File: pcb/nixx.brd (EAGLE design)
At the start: 20 x 40 mm, 43 parts, among them IC1 24C64ST

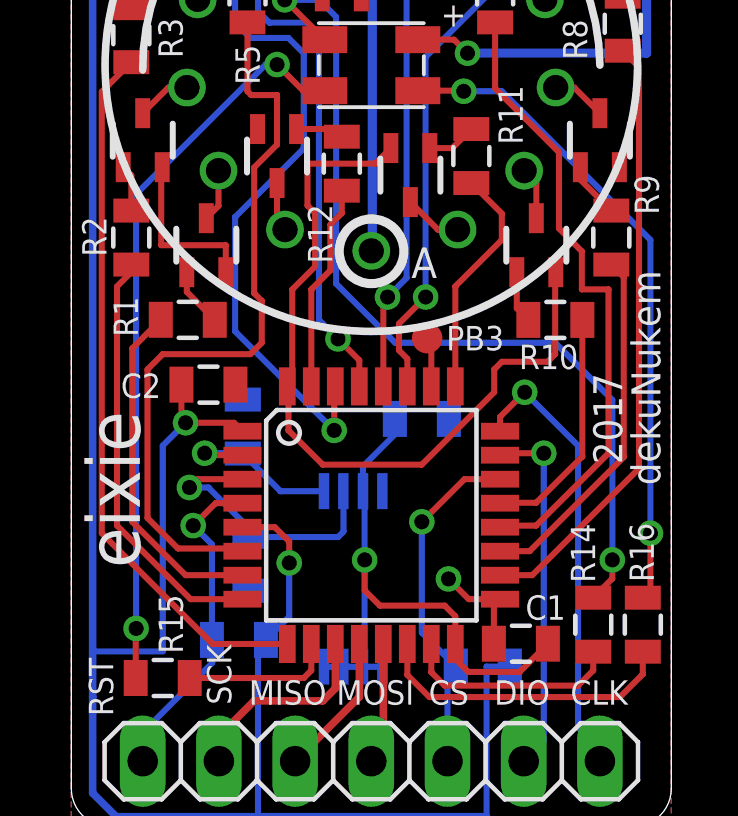
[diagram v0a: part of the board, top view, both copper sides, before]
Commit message: using NSS, SPI test
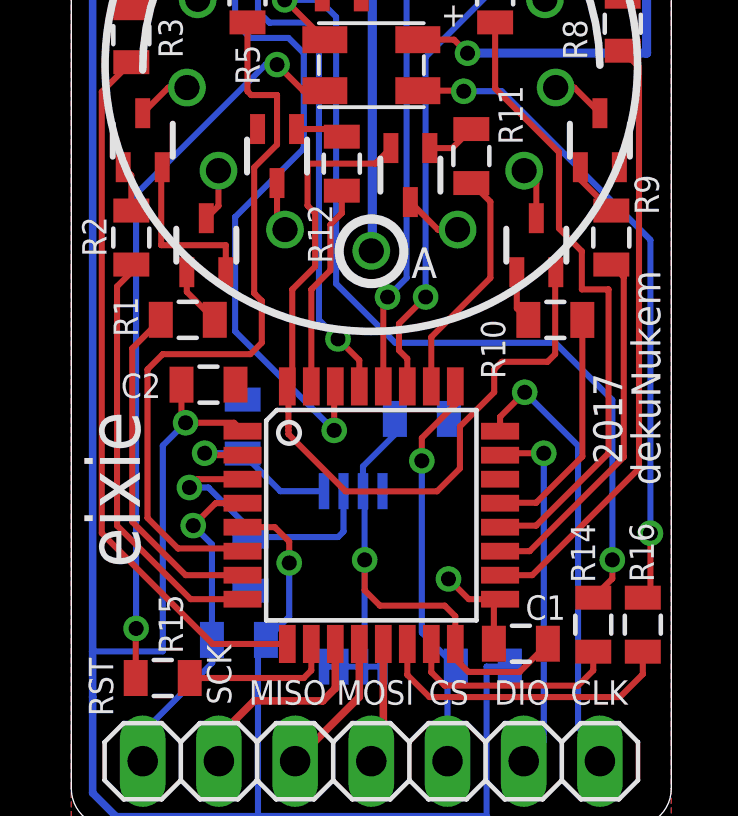
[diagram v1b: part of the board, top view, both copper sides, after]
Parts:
- removed TP3: TEST-POINT3X4, joyAnalog:PAD.03X.04
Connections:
- removed net N$17: TP3.P$1, U$2.26
- net SPI_CS: now also U$2.25; no longer U$2.22
- net STM_DOT_LEFT: now also U$2.26; no longer U$2.25
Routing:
- net SPI_CS: track 11.8 -> 13.6 mm
- net N$17: track 1.67 -> 0.00 mm
- net GND: track 57.0 -> 58.6 mm
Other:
- board text removed: "PB3"
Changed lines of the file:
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@@
 <circle x="10.0076" y="19.177" radius="1.077628125" width="0.3048" layer="21"/>
 <text x="12.192" y="19.304" size="1.016" layer="25" rot="R180">A</text>
-<text x="12.4968" y="15.875" size="0.8128" layer="25">PB3</text>
 <text x="17.018" y="34.671" size="1.143" layer="25">G</text>
 <text x="18.669" y="18.542" size="0.9652" layer="25" rot="R270">dekuNukem</text>
@@
 </element>
 <element name="R10" library="joyAnalog" package="0805" value="" x="16.135" y="16.889" smashed="yes" rot="R180">
-<attribute name="NAME" x="16.897" y="16.0635" size="0.8128" layer="25" rot="R180"/>
+<attribute name="NAME" x="13.6545" y="16.897" size="0.8128" layer="25" rot="R270"/>
 <attribute name="VALUE" x="17.151" y="18.286" size="0.4064" layer="27" rot="R180"/>
 <attribute name="VALUE" x="17.151" y="18.286" size="0.4064" layer="27" rot="R180"/>
@@
 <attribute name="VALUE" x="17.653" y="7.747" size="0.4064" layer="27" rot="R270"/>
 </element>
-<element name="TP3" library="joyAnalog" package="PAD.03X.04" value="TEST-POINT3X4" x="11.8618" y="16.2814" smashed="yes"/>
 <element name="R17" library="joyAnalog" package="0805" value="" x="5.588" y="6.223" smashed="yes" rot="MR180">
 <attribute name="NAME" x="4.7244" y="5.2197" size="0.8128" layer="26" rot="MR180"/>
@@
 <wire x1="13.2334" y1="5.1562" x2="12.8" y2="5.5896" width="0.2032" layer="1"/>
 <wire x1="12.8" y1="5.5896" x2="12.8" y2="6.0884" width="0.2032" layer="1"/>
-<wire x1="14.097" y1="14.478" x2="11.684" y2="12.065" width="0.2032" layer="1"/>
-<wire x1="11.684" y1="12.065" x2="8.382" y2="12.065" width="0.2032" layer="1"/>
-<wire x1="8.382" y1="12.065" x2="7.239" y2="13.208" width="0.2032" layer="1"/>
-<wire x1="7.239" y1="13.208" x2="7.239" y2="14.605" width="0.2032" layer="1"/>
+<wire x1="7.239" y1="13.208" x2="7.239" y2="13.335" width="0.2032" layer="1"/>
+<wire x1="7.239" y1="13.335" x2="7.239" y2="14.605" width="0.2032" layer="1"/>
 <wire x1="7.239" y1="14.605" x2="7.239" y2="14.6346" width="0.2032" layer="1"/>
 <wire x1="7.239" y1="14.6346" x2="7.2" y2="14.6736" width="0.2032" layer="1"/>
@@
 <wire x1="9.723" y1="12.009" x2="10.784" y2="13.07" width="0.2032" layer="16"/>
 <wire x1="10.784" y1="13.07" x2="10.784" y2="13.589" width="0.2032" layer="16"/>
+<wire x1="14.097" y1="14.478" x2="12.954" y2="13.335" width="0.2032" layer="1"/>
+<wire x1="12.954" y1="13.335" x2="12.954" y2="11.938" width="0.2032" layer="1"/>
+<wire x1="12.954" y1="11.938" x2="12.192" y2="11.176" width="0.2032" layer="1"/>
+<wire x1="12.192" y1="11.176" x2="9.144" y2="11.176" width="0.2032" layer="1"/>
+<wire x1="9.144" y1="11.176" x2="7.239" y2="13.081" width="0.2032" layer="1"/>
+<wire x1="7.239" y1="13.081" x2="7.239" y2="13.208" width="0.2032" layer="1"/>
 <wire x1="9.779" y1="5.401" x2="9.723" y2="5.33" width="0" layer="19" extent="16-16"/>
 </signal>
@@
 <signal name="SPI_CS">
 <contactref element="JP2" pad="5"/>
-<contactref element="U$2" pad="22"/>
-<via x="11.684" y="10.16" extent="1-16" drill="0.5"/>
 <contactref element="R18" pad="1"/>
-<wire x1="14.2926" y1="11.581" x2="13.105" y2="11.581" width="0.2032" layer="1"/>
-<wire x1="13.105" y1="11.581" x2="11.684" y2="10.16" width="0.2032" layer="1"/>
-<wire x1="11.684" y1="10.16" x2="11.684" y2="6.466" width="0.2032" layer="16"/>
+<wire x1="11.684" y1="12.192" x2="11.684" y2="6.466" width="0.2032" layer="16"/>
 <wire x1="11.684" y1="6.466" x2="12.816" y2="5.334" width="0.2032" layer="16"/>
 <wire x1="12.54" y1="2.181" x2="12.54" y2="5.058" width="0.2032" layer="16"/>
 <wire x1="12.54" y1="5.058" x2="12.816" y2="5.334" width="0.2032" layer="16"/>
+<contactref element="U$2" pad="25"/>
+<via x="11.684" y="12.192" extent="1-16" drill="0.5"/>
+<wire x1="11.684" y1="12.192" x2="11.684" y2="12.954" width="0.2032" layer="1"/>
+<wire x1="11.684" y1="12.954" x2="12.827" y2="14.097" width="0.2032" layer="1"/>
+<wire x1="12.827" y1="14.097" x2="12.827" y2="14.6466" width="0.2032" layer="1"/>
+<wire x1="12.827" y1="14.6466" x2="12.8" y2="14.6736" width="0.2032" layer="1"/>
 </signal>
 <signal name="SWD_DIO">
@@
 <signal name="STM_DOT_LEFT">
 <contactref element="R11" pad="1"/>
-<contactref element="U$2" pad="25"/>
-<wire x1="12.8" y1="14.6736" x2="12.8" y2="18.007" width="0.2032" layer="1"/>
-<wire x1="12.8" y1="18.007" x2="14.351" y2="19.558" width="0.2032" layer="1"/>
-<wire x1="14.351" y1="19.558" x2="14.351" y2="20.436" width="0.2032" layer="1"/>
-<wire x1="14.351" y1="20.436" x2="13.335" y2="21.452" width="0.2032" layer="1"/>
+<contactref element="U$2" pad="26"/>
+<wire x1="12" y1="14.6736" x2="12" y2="16.318" width="0.2032" layer="1"/>
+<wire x1="12" y1="16.318" x2="13.97" y2="18.288" width="0.2032" layer="1"/>
+<wire x1="13.335" y1="21.452" x2="13.346" y2="21.452" width="0.2032" layer="1"/>
+<wire x1="13.346" y1="21.452" x2="13.97" y2="20.828" width="0.2032" layer="1"/>
+<wire x1="13.97" y1="20.828" x2="13.97" y2="18.288" width="0.2032" layer="1"/>
 </signal>
 <signal name="STM_DOT_RIGHT">
@@
 <wire x1="2.032" y1="15.943" x2="2.982" y2="16.893" width="0.2032" layer="1"/>
 </signal>
-<signal name="N$17">
-<contactref element="U$2" pad="26"/>
-<contactref element="TP3" pad="P$1"/>
-<wire x1="12" y1="14.6736" x2="12" y2="16.1432" width="0.2032" layer="1"/>
-<wire x1="12" y1="16.1432" x2="11.8618" y2="16.2814" width="0.2032" layer="1"/>
-</signal>
 <signal name="N$21">

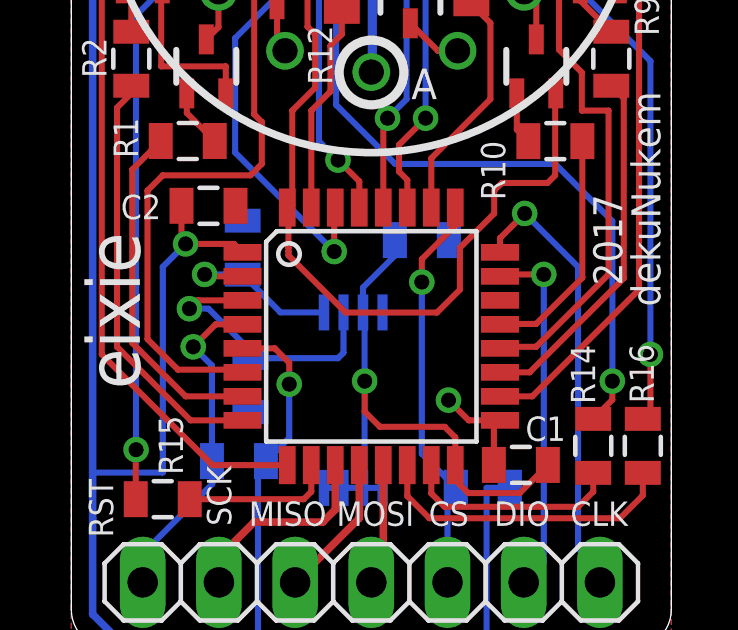
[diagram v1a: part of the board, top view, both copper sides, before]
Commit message: PA12 testpoint
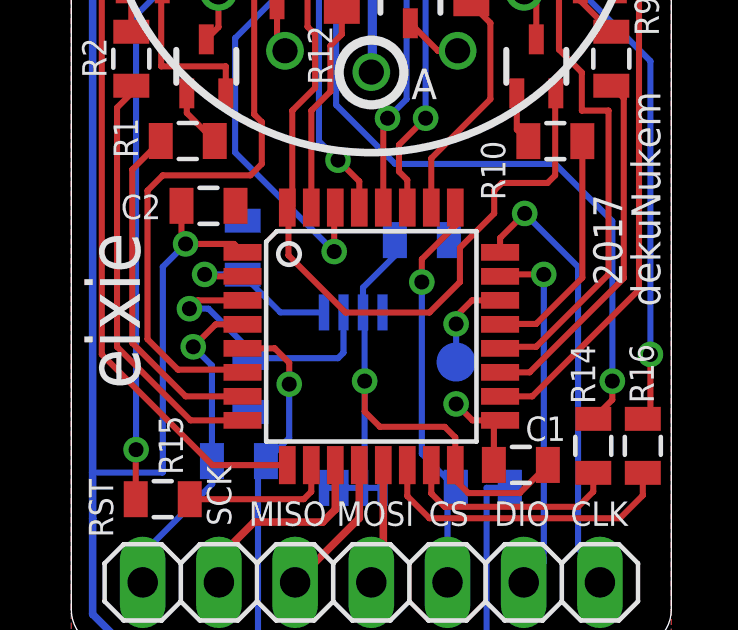
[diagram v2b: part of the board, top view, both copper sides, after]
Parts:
- added TP1: PTR1TP13R, testpad:TP13R
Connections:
- new net N$17: TP1.TP, U$2.22
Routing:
- net N$17: track 0.00 -> 3.21 mm, vias 0 -> 1
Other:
- board text added: "PA12"
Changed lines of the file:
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@@
 <text x="17.399" y="15.113" size="0.9652" layer="25" rot="R270">2017</text>
 <text x="0.508" y="13.843" size="1.778" layer="25" rot="R270">eixie</text>
+<text x="13.97" y="8.255" size="0.8128" layer="26" rot="MR90">PA12</text>
 </plain>
 <attributes>
@@
 <attribute name="VALUE" x="4.318" y="12.319" size="0.4064" layer="28" rot="MR90"/>
 </element>
+<element name="TP1" library="testpad" package="TP13R" value="PTR1TP13R" x="12.827" y="9.525" smashed="yes" rot="MR0">
+<attribute name="TP_SIGNAL_NAME" value="" x="12.827" y="6.985" size="1" layer="38" rot="MR0"/>
+</element>
 </elements>
 <signals>
@@
 <wire x1="13.2334" y1="5.1562" x2="12.8" y2="5.5896" width="0.2032" layer="1"/>
 <wire x1="12.8" y1="5.5896" x2="12.8" y2="6.0884" width="0.2032" layer="1"/>
-<wire x1="7.239" y1="13.208" x2="7.239" y2="13.335" width="0.2032" layer="1"/>
-<wire x1="7.239" y1="13.335" x2="7.239" y2="14.605" width="0.2032" layer="1"/>
+<wire x1="7.239" y1="13.081" x2="7.239" y2="14.605" width="0.2032" layer="1"/>
 <wire x1="7.239" y1="14.605" x2="7.239" y2="14.6346" width="0.2032" layer="1"/>
 <wire x1="7.239" y1="14.6346" x2="7.2" y2="14.6736" width="0.2032" layer="1"/>
@@
 <wire x1="10.784" y1="13.07" x2="10.784" y2="13.589" width="0.2032" layer="16"/>
 <wire x1="14.097" y1="14.478" x2="12.954" y2="13.335" width="0.2032" layer="1"/>
-<wire x1="12.954" y1="13.335" x2="12.954" y2="11.938" width="0.2032" layer="1"/>
-<wire x1="12.954" y1="11.938" x2="12.192" y2="11.176" width="0.2032" layer="1"/>
-<wire x1="12.192" y1="11.176" x2="9.144" y2="11.176" width="0.2032" layer="1"/>
 <wire x1="9.144" y1="11.176" x2="7.239" y2="13.081" width="0.2032" layer="1"/>
-<wire x1="7.239" y1="13.081" x2="7.239" y2="13.208" width="0.2032" layer="1"/>
+<wire x1="12.954" y1="13.335" x2="12.954" y2="12.192" width="0.2032" layer="1"/>
+<wire x1="12.954" y1="12.192" x2="11.938" y2="11.176" width="0.2032" layer="1"/>
+<wire x1="11.938" y1="11.176" x2="9.144" y2="11.176" width="0.2032" layer="1"/>
 <wire x1="9.779" y1="5.401" x2="9.723" y2="5.33" width="0" layer="19" extent="16-16"/>
 </signal>
@@
 <contactref element="D1" pad="1"/>
 <via x="7.2644" y="8.7884" extent="1-16" drill="0.5"/>
-<via x="12.573" y="8.255" extent="1-16" drill="0.5"/>
+<via x="12.827" y="8.128" extent="1-16" drill="0.5"/>
 <via x="3.81" y="13.462" extent="1-16" drill="0.5"/>
 <via x="13.208" y="25.781" extent="1-16" drill="0.5"/>
 <wire x1="11.55" y1="26.231" x2="12.758" y2="26.231" width="0.2032" layer="1"/>
 <wire x1="12.758" y1="26.231" x2="13.208" y2="25.781" width="0.2032" layer="1"/>
-<wire x1="12.573" y1="8.255" x2="13.247" y2="7.581" width="0.2032" layer="1"/>
-<wire x1="13.247" y1="7.581" x2="14.2926" y2="7.581" width="0.2032" layer="1"/>
 <wire x1="14.2926" y1="7.581" x2="14.086" y2="7.3744" width="0.2032" layer="1"/>
 <wire x1="14.086" y1="7.3744" x2="14.086" y2="6.096" width="0.2032" layer="1"/>
@@
 <wire x1="14.616" y1="5.334" x2="13.843" y2="5.334" width="0.2032" layer="16"/>
 <wire x1="13.843" y1="5.334" x2="13.843" y2="0.3302" width="0.2032" layer="16"/>
+<wire x1="14.2926" y1="7.581" x2="13.374" y2="7.581" width="0.2032" layer="1"/>
+<wire x1="13.374" y1="7.581" x2="12.827" y2="8.128" width="0.2032" layer="1"/>
 </signal>
 <signal name="SPI_SCK">
@@
 <wire x1="5.98" y1="9.652" x2="5.969" y2="9.663" width="0.2032" layer="16"/>
 </signal>
+<signal name="N$17">
+<contactref element="U$2" pad="22"/>
+<contactref element="TP1" pad="TP"/>
+<via x="12.827" y="10.795" extent="1-16" drill="0.5"/>
+<wire x1="14.2926" y1="11.581" x2="13.359" y2="11.581" width="0.2032" layer="1"/>
+<wire x1="13.359" y1="11.581" x2="12.827" y2="11.049" width="0.2032" layer="1"/>
+<wire x1="12.827" y1="11.049" x2="12.827" y2="10.795" width="0.2032" layer="1"/>
+<wire x1="12.827" y1="9.525" x2="12.827" y2="10.795" width="0.2032" layer="16"/>
+</signal>
 </signals>

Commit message: updated text and miter
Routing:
- net +3V3: track 117.6 -> 117.1 mm
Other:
- outline, holes or cut-outs redrawn

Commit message: started firmware
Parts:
- added R21: (no value), joyAnalog:0805
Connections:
- net GND: now also R21.1
- net STM_DOT_RIGHT: now also R21.2
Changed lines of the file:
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@@
 <attribute name="TP_SIGNAL_NAME" value="" x="12.827" y="6.985" size="1" layer="38" rot="MR0"/>
 </element>
+<element name="R21" library="joyAnalog" package="0805" value="" x="-6.731" y="-3.429"/>
 </elements>
 <signals>
@@
 <wire x1="12.954" y1="12.192" x2="11.938" y2="11.176" width="0.2032" layer="1"/>
 <wire x1="11.938" y1="11.176" x2="9.144" y2="11.176" width="0.2032" layer="1"/>
-<wire x1="9.779" y1="5.401" x2="9.723" y2="5.33" width="0" layer="19" extent="16-16"/>
+<contactref element="R21" pad="1"/>
+<wire x1="15.0546" y1="37.7508" x2="17.5946" y2="37.7508" width="0" layer="19" extent="1-1"/>
+<wire x1="13.461" y1="33.666" x2="15.0546" y2="37.7508" width="0" layer="19" extent="1-1"/>
+<wire x1="12.584" y1="29.352" x2="13.461" y2="33.666" width="0" layer="19" extent="1-1"/>
+<wire x1="9.667" y1="27.675" x2="12.584" y2="29.352" width="0" layer="19" extent="1-1"/>
+<wire x1="10.653" y1="22.617" x2="9.667" y2="27.675" width="0" layer="19" extent="1-1"/>
+<wire x1="9.723" y1="11.18" x2="9.144" y2="11.176" width="0" layer="19" extent="1-16"/>
+<wire x1="9.723" y1="5.33" x2="9.779" y2="5.401" width="0" layer="19" extent="16-16"/>
+<wire x1="5.472" y1="14.732" x2="7.2" y2="14.6736" width="0" layer="19" extent="1-1"/>
+<wire x1="6.208" y1="23.252" x2="7.874" y2="22.098" width="0" layer="19" extent="1-1"/>
+<wire x1="5.15" y1="18.481" x2="7.366" y2="17.907" width="0" layer="19" extent="1-1"/>
+<wire x1="18.269" y1="21.981" x2="16.15" y2="18.481" width="0" layer="19" extent="1-1"/>
+<wire x1="7.366" y1="32.512" x2="9.667" y2="27.675" width="0" layer="19" extent="1-1"/>
+<wire x1="1.27" y1="31.612" x2="3.926" y2="31.274" width="0" layer="19" extent="1-1"/>
+<wire x1="1.6" y1="28.731" x2="1.27" y2="31.612" width="0" layer="19" extent="1-1"/>
+<wire x1="18.4" y1="30.031" x2="12.584" y2="29.352" width="0" layer="19" extent="1-1"/>
+<wire x1="-7.631" y1="-3.429" x2="8.423" y2="5.33" width="0" layer="19" extent="1-16"/>
 </signal>
 <signal name="N$1">
@@
 <wire x1="8.636" y1="20.066" x2="8.636" y2="18.542" width="0.2032" layer="1"/>
 <wire x1="8.636" y1="18.542" x2="8.001" y2="17.907" width="0.2032" layer="1"/>
+<contactref element="R21" pad="2"/>
+<wire x1="-5.831" y1="-3.429" x2="8.001" y2="14.6746" width="0" layer="19" extent="1-1"/>
 </signal>
 <signal name="STM_6">

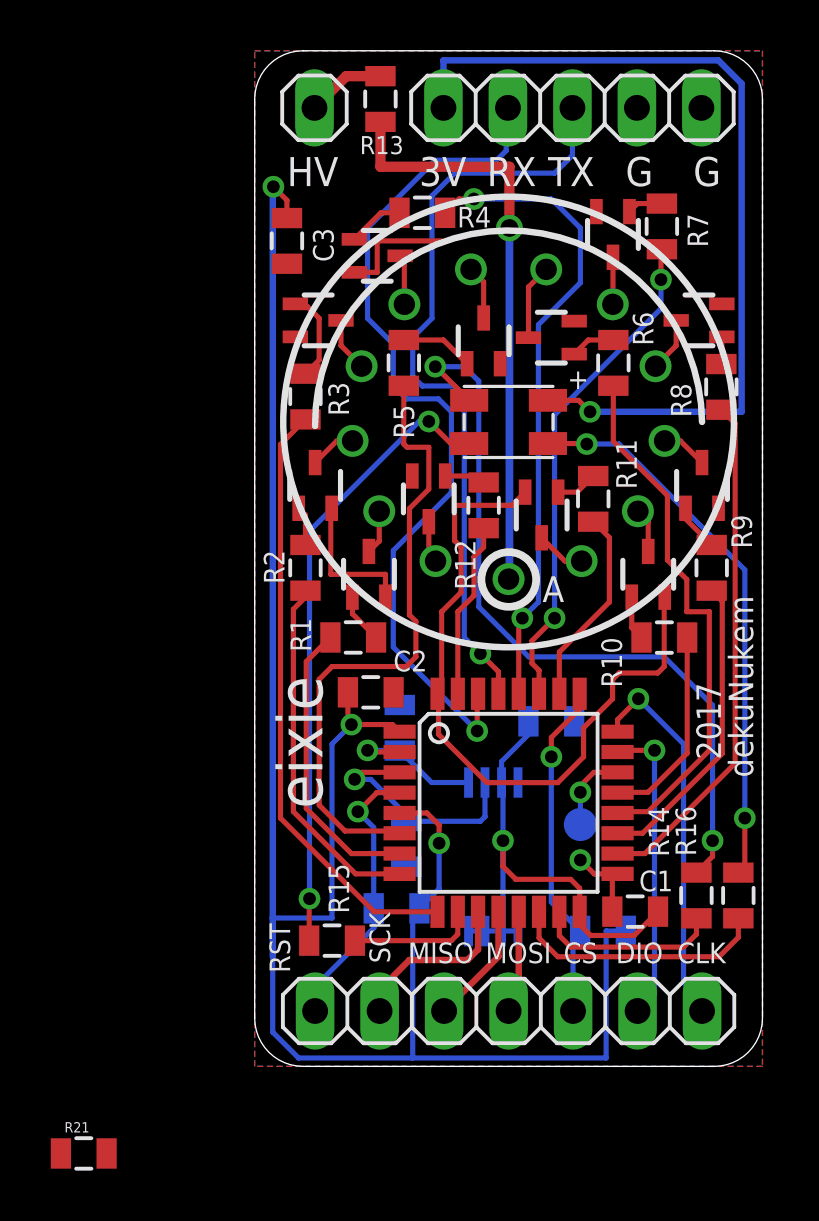
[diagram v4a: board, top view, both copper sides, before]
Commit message: added pulldown on BOOT0
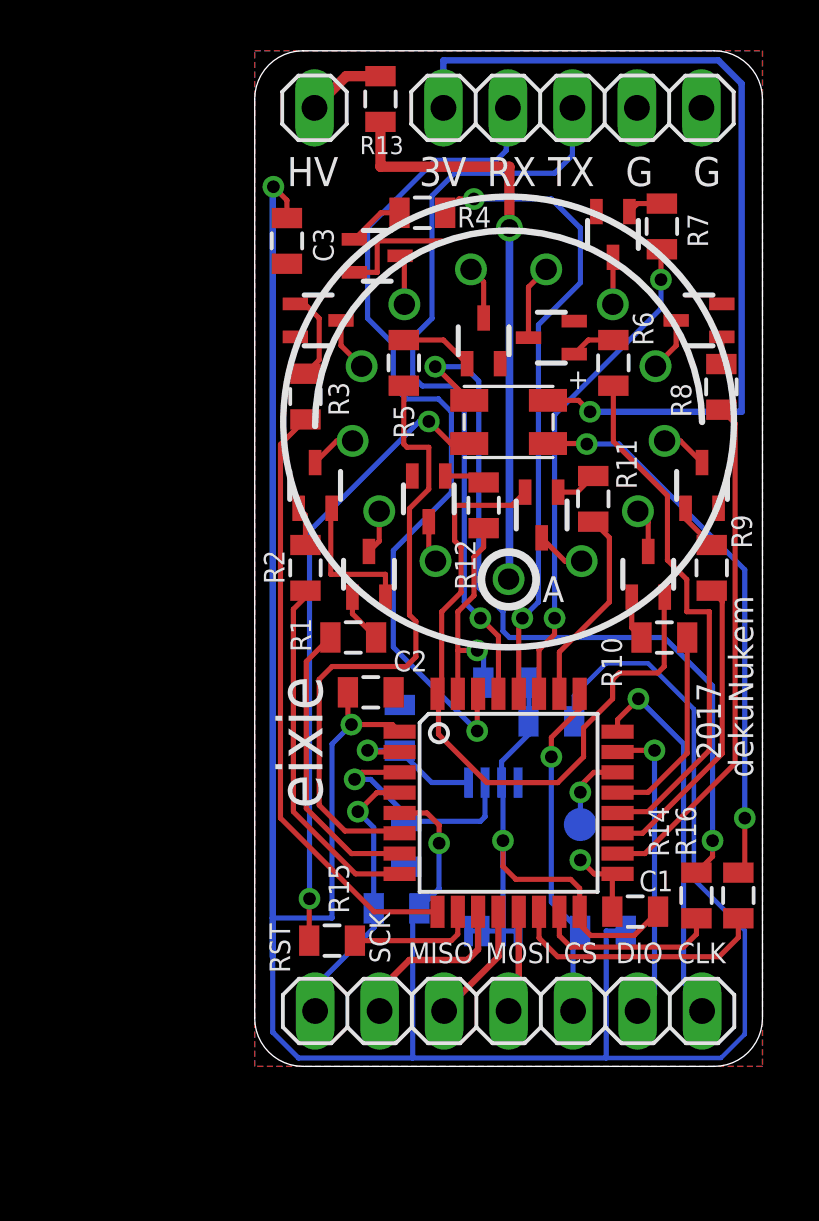
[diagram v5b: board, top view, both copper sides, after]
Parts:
- C1: value (none) -> 1uF
- C2, C3, C4: value (none) -> 100nF
- R1, R10, R11, R12, R17, R18, R19, R2, R20, R3, R4, R5, R6, R7, R8, R9: value (none) -> 4K7
- R13, R21: value (none) -> 10K
- R14, R15: value (none) -> 470
- R16: value (none) -> 0
- moved R21 24.9 mm to (9.91, 15.1), flipped to the bottom
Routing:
- net +3V3: track 117.1 -> 143.6 mm
- net STM_DOT_RIGHT: track 6.95 -> 9.09 mm, vias 0 -> 1
- net GND: track 58.4 -> 60.0 mm
